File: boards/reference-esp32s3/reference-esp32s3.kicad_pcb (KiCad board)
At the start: 2 copper layers, 30 x 40 mm, 4 parts

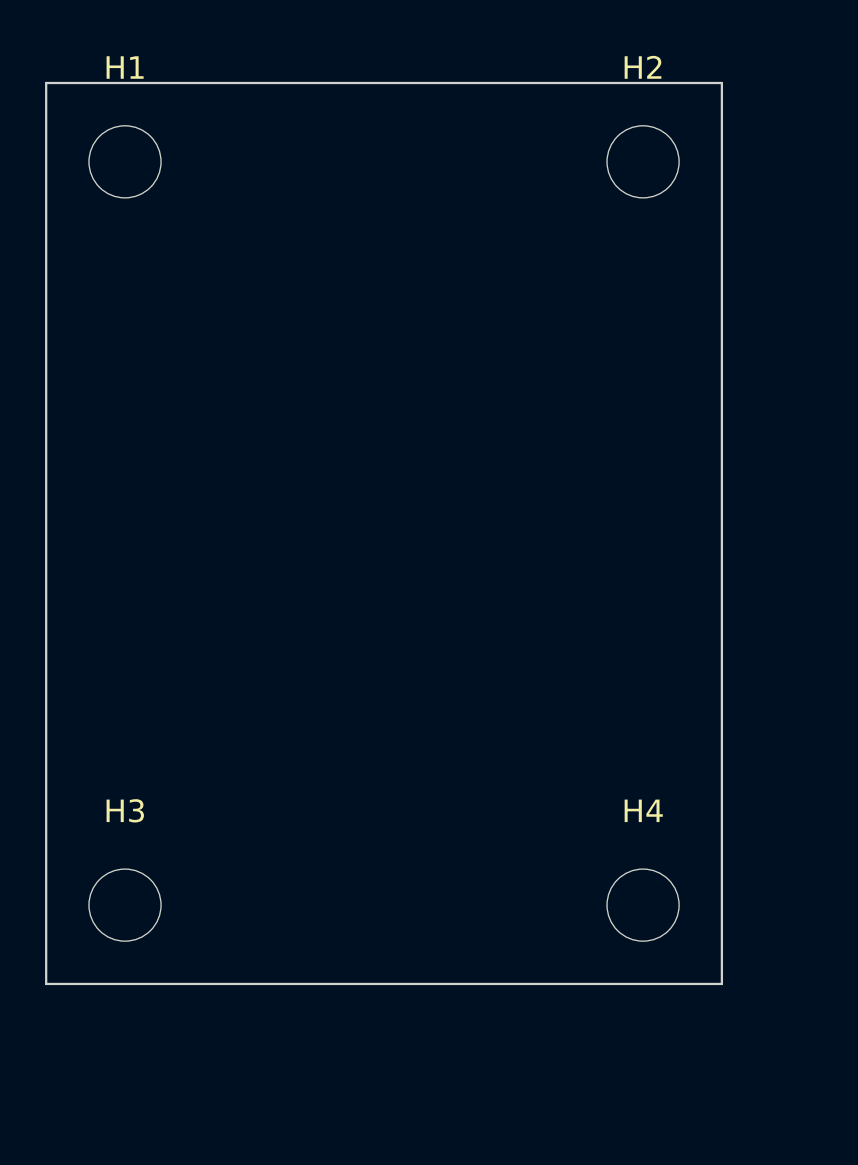
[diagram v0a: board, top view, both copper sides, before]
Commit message: Place registry-bound components; BOM resolves to OpenPartsCore; DRC clean
Footprints carry an opc_id field so the BOM is resolved from the design, not reconstructed from designators; unresolved ids write no BOM. Placing components surfaced 27 real DRC violations - the module's 0.2mm thermal vias vs KiCad's 0.3mm default, and mounting holes inside the antenna keepout. Fixed by setting min through-drill to 0.2mm deliberately and by measuring the keepout (full width, up to y=13.25) then moving the upper hole pair below it; board grew to 34x46. kicad-cli pcb drc --severity-error: 0 violations. Bridge re-verified: ODC run 4 fits an enclosure to the populated board. Still no schematic, so no nets.
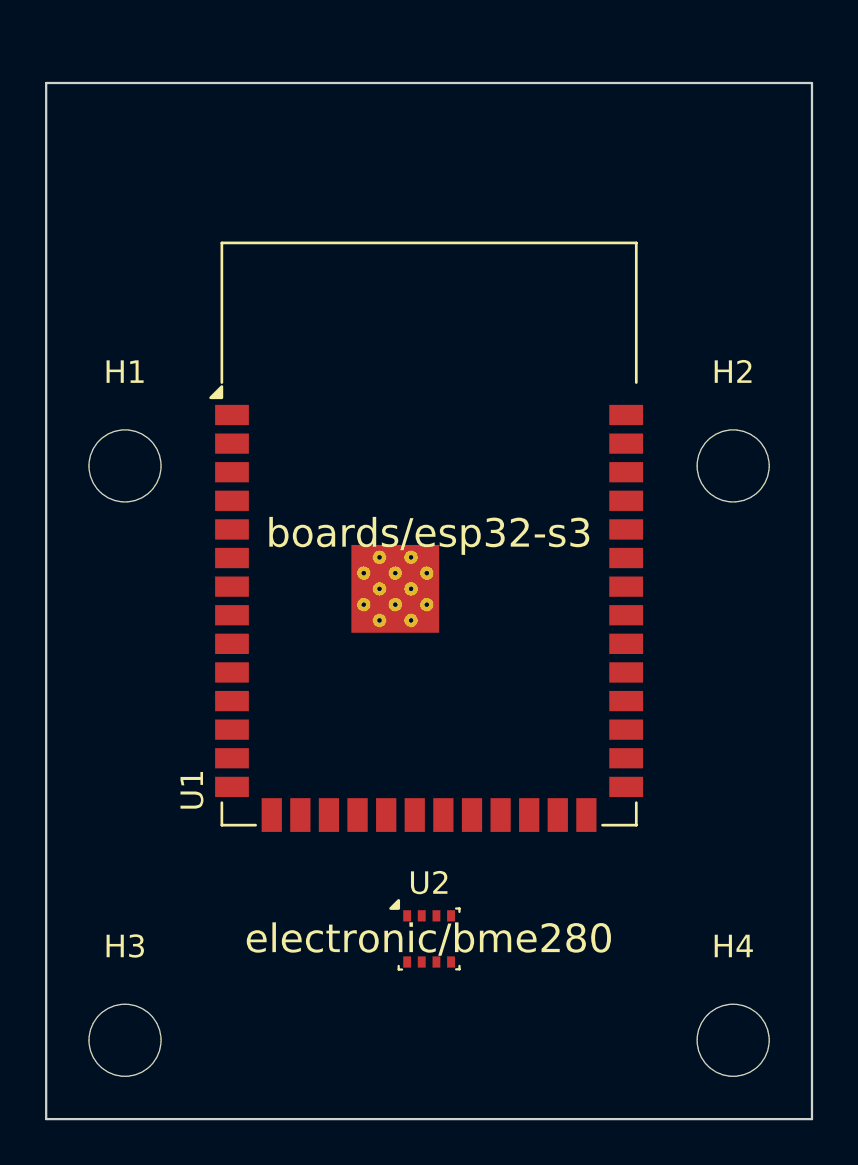
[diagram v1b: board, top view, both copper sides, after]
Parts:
- added U1: ESP32-S3-WROOM-1, ESP32-S3-WROOM-1, F.Cu at (17.0, 20.0)
- added U2: BME280, Bosch_LGA-8_2.5x2.5mm_P0.65mm_ClockwisePinNumbering, F.Cu at (17.0, 38.0)
- moved H2 14.1 mm to (30.5, 17.0)
- moved H1 13.5 mm to (3.50, 17.0)
- moved H4 7.21 mm to (30.5, 42.5)
- moved H3 6.00 mm to (3.50, 42.5)
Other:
- board size 30 x 40 mm -> 34 x 46 mm
